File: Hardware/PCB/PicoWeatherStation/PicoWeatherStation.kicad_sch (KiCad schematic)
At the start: 40 parts, among them J1 TOUCH_PANEL, J2 LCD_BL, Q1 AO3400A, SW1 SW_PICO_RST, U1 Pico, U2 XPT2046, U3 nRF24L01+, U4 GY-BME280

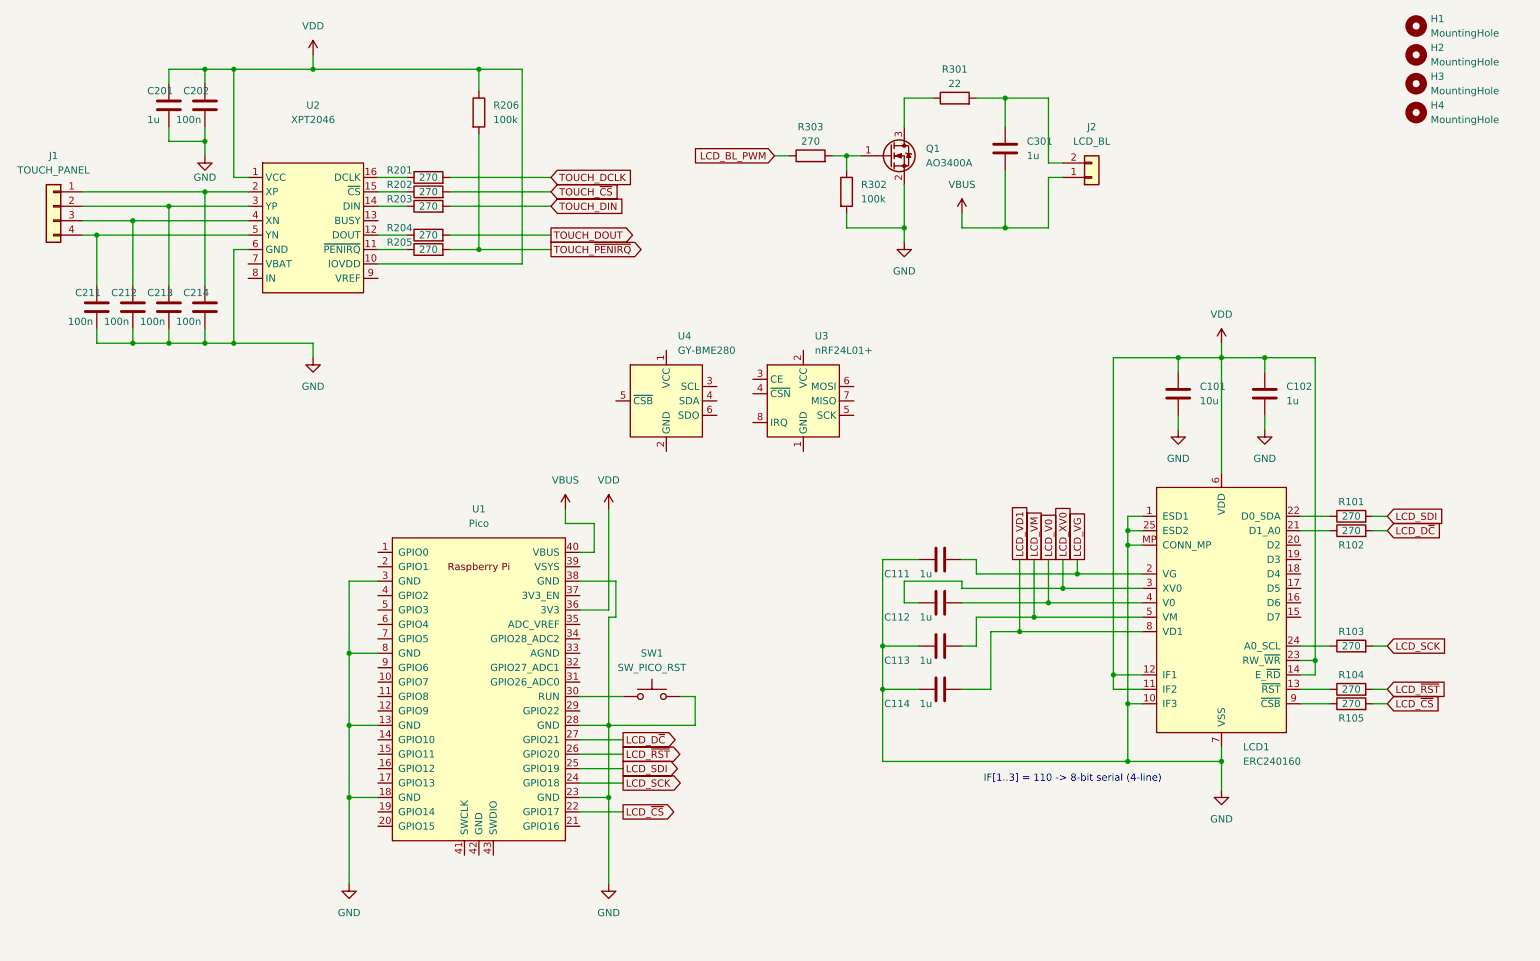
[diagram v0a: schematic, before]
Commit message: Fully wire up the PCB
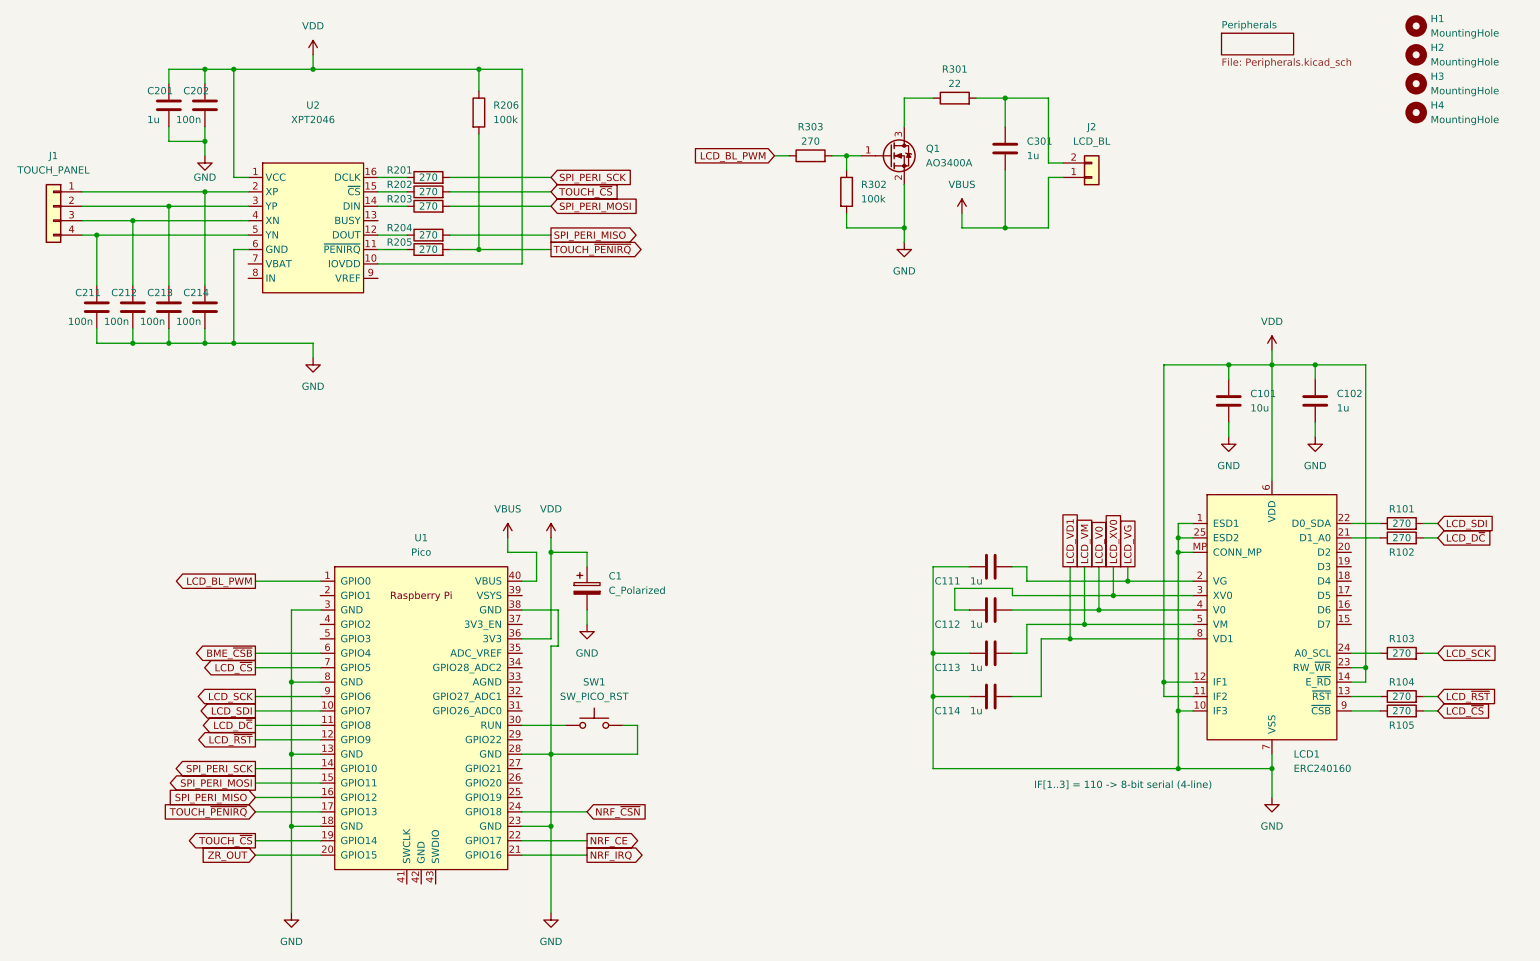
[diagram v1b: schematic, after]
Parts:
- removed U3: nRF24L01+, PicoWeatherStation:nRF24L01+, symbol PicoWeatherStation:nRF24L01+
- removed U4: GY-BME280, PicoWeatherStation:GY-BME280, symbol PicoWeatherStation:GY-BME280
- added C1: C_Polarized, Capacitor_SMD:CP_Elec_5x5.4, symbol Device:C_Polarized
- H1, H2, H3, H4: footprint MountingHole:MountingHole_3.2mm_M3_Pad_Via -> MountingHole:MountingHole_2.7mm_Pad_Via
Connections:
- net TOUCH_DCLK is gone; now on net SPI_PERI_SCK: R201.2
- net TOUCH_DIN is gone; now on net SPI_PERI_MOSI: R203.2
- net TOUCH_DOUT is gone; now on net SPI_PERI_MISO: R204.2
- net GND: now also C1.2
- net LCD_BL_PWM: now also U1.1 (GPIO0)
- net LCD_D~{C}: now also U1.11 (GPIO8); no longer U1.27 (GPIO21)
- net LCD_SCK: now also U1.9 (GPIO6); no longer U1.24 (GPIO18)
- net LCD_SDI: now also U1.10 (GPIO7); no longer U1.25 (GPIO19)
- net LCD_~{CS}: now also U1.7 (GPIO5); no longer U1.22 (GPIO17)
- net LCD_~{RST}: now also U1.12 (GPIO9); no longer U1.26 (GPIO20)
- net TOUCH_~{CS}: now also U1.19 (GPIO14)
- net TOUCH_~{PENIRQ}: now also U1.17 (GPIO13)
- net VDD: now also C1.1
- net SPI_PERI_SCK: now reaches U1.14 (GPIO10)
- net SPI_PERI_MOSI: now reaches U1.15 (GPIO11)
- net SPI_PERI_MISO: now reaches U1.16 (GPIO12)
- net ZR_OUT: now reaches U1.20 (GPIO15)
- net NRF_IRQ: now reaches U1.21 (GPIO16)
- net BME_~{CSB}: now reaches U1.6 (GPIO4)
- new net NRF_CE: U1.22 (GPIO17)
- new net NRF_~{CSN}: U1.24 (GPIO18)
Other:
- added sheet Peripherals (Peripherals.kicad_sch)
- moved on the sheet: C101, C102, C111, C112, C113, C114, LCD1, R101, R102, R103, R104, R105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

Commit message: Update the PCB
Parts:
- added R207: 270, Resistor_SMD:R_0805_2012Metric_Pad1.20x1.40mm_HandSolder, symbol Device:R
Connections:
- net ZR_OUT: now also U1.25 (GPIO19); no longer U1.20 (GPIO15)
- net at U2.13 (BUSY): now also R207.1
- new net TOUCH_BUSY: R207.2, U1.20 (GPIO15)
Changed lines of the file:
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@@
+    (stroke (width 0) (type default) (color 0 0 0 0))
+  )
+  (wire (pts (xy 106.68 153.67) (xy 118.11 153.67))
     (stroke (width 0) (type default) (color 0 0 0 0))
   )
@@
     (stroke (width 0) (type default) (color 0 0 0 0))
   )
+  (wire (pts (xy 81.28 52.07) (xy 86.36 52.07))
+    (stroke (width 0) (type default) (color 0 0 0 0))
+  )
   (wire (pts (xy 55.88 44.45) (xy 58.42 44.45))
     (stroke (width 0) (type default) (color 0 0 0 0))
@@
   )
   (wire (pts (xy 59.69 138.43) (xy 71.12 138.43))
+    (stroke (width 0) (type default) (color 0 0 0 0))
+  )
+  (wire (pts (xy 93.98 52.07) (xy 111.76 52.07))
     (stroke (width 0) (type default) (color 0 0 0 0))
   )
@@
     (effects (font (size 1.27 1.27)) (justify left bottom))
   )
-  (global_label "ZR_OUT" (shape input) (at 59.69 163.83 180) (fields_autoplaced)
+  (global_label "TOUCH_BUSY" (shape input) (at 59.69 163.83 180) (fields_autoplaced)
     (effects (font (size 1.27 1.27)) (justify right))
-    (property "Intersheet References" "${INTERSHEET_REFS}" (id 0) (at 50.2012 163.7506 0)
+    (property "Intersheet References" "${INTERSHEET_REFS}" (id 0) (at 45.1817 163.7506 0)
       (effects (font (size 1.27 1.27)) (justify right) hide)
     )
@@
     )
   )
+  (global_label "ZR_OUT" (shape input) (at 118.11 153.67 0) (fields_autoplaced)
+    (effects (font (size 1.27 1.27)) (justify left))
+    (property "Intersheet References" "${INTERSHEET_REFS}" (id 0) (at 127.5988 153.5906 0)
+      (effects (font (size 1.27 1.27)) (justify left) hide)
+    )
+  )
   (global_label "LCD_~{CS}" (shape input) (at 267.97 138.43 0) (fields_autoplaced)
     (effects (font (size 1.27 1.27)) (justify left))
@@
     (property "Intersheet References" "${INTERSHEET_REFS}" (id 0) (at 49.294 143.5894 0)
       (effects (font (size 1.27 1.27)) (justify right) hide)
+    )
+  )
+  (global_label "TOUCH_BUSY" (shape output) (at 111.76 52.07 0) (fields_autoplaced)
+    (effects (font (size 1.27 1.27)) (justify left))
+    (property "Intersheet References" "${INTERSHEET_REFS}" (id 0) (at 126.2683 51.9906 0)
+      (effects (font (size 1.27 1.27)) (justify left) hide)
     )
   )
@@
     )
     (property "Datasheet" "~" (id 3) (at 261.62 128.27 0)
+      (effects (font (size 1.27 1.27)) hide)
+    )
+    (pin "1")
+    (pin "2")
+  )
+  (symbol (lib_id "Device:R") (at 90.17 52.07 90) (unit 1)
+    (in_bom yes) (on_board yes)
+    (property "Reference" "R207" (id 0) (at 85.09 50.8 90))
+    (property "Value" "270" (id 1) (at 90.17 52.07 90))
+    (property "Footprint" "Resistor_SMD:R_0805_2012Metric_Pad1.20x1.40mm_HandSolder" (id 2) (at 90.17 53.848 90)
+      (effects (font (size 1.27 1.27)) hide)
+    )
+    (property "Datasheet" "~" (id 3) (at 90.17 52.07 0)
       (effects (font (size 1.27 1.27)) hide)
     )
@@
       (reference "R206") (unit 1) (value "100k") (footprint "Resistor_SMD:R_0805_2012Metric_Pad1.20x1.40mm_HandSolder")
     )
+    (path "/72400bf9-1560-4fc0-8dfb-0f046ef29e65"
+      (reference "R207") (unit 1) (value "270") (footprint "Resistor_SMD:R_0805_2012Metric_Pad1.20x1.40mm_HandSolder")
+    )
     (path "/8d763b0e-f6bf-4795-b6af-c73111e487f6"
       (reference "R301") (unit 1) (value "22") (footprint "Resistor_SMD:R_0805_2012Metric_Pad1.20x1.40mm_HandSolder")
@@
       (reference "SW1") (unit 1) (value "SW_PICO_RST") (footprint "Button_Switch_SMD:SW_Push_1P1T_NO_6x6mm_H9.5mm")
     )
+    (path "/8ed95ab6-c4d7-41f9-a767-b1e59c08f8aa/0dd8649c-8f2a-4391-b233-72bf55db379f"
+      (reference "SW2") (unit 1) (value "SW_PICO_RST") (footprint "Button_Switch_SMD:SW_Push_1P1T_NO_6x6mm_H9.5mm")
+    )
+    (path "/8ed95ab6-c4d7-41f9-a767-b1e59c08f8aa/ee07d6f4-6422-4982-b2c3-95f2866c5416"
+      (reference "SW3") (unit 1) (value "SW_PICO_RST") (footprint "Button_Switch_SMD:SW_Push_1P1T_NO_6x6mm_H9.5mm")
+    )
+    (path "/8ed95ab6-c4d7-41f9-a767-b1e59c08f8aa/31382075-085e-4e4a-ad7d-7fed5235aaa9"
+      (reference "SW4") (unit 1) (value "SW_PICO_RST") (footprint "Button_Switch_SMD:SW_Push_1P1T_NO_6x6mm_H9.5mm")
+    )
+    (path "/8ed95ab6-c4d7-41f9-a767-b1e59c08f8aa/e65e769d-e377-426b-848d-7c3769842a4d"
+      (reference "SW5") (unit 1) (value "SW_PICO_RST") (footprint "Button_Switch_SMD:SW_Push_1P1T_NO_6x6mm_H9.5mm")
+    )
+    (path "/8ed95ab6-c4d7-41f9-a767-b1e59c08f8aa/b6a0dc04-656d-4f3b-9f9e-ff27f7ab450f"
+      (reference "SW6") (unit 1) (value "SW_PICO_RST") (footprint "Button_Switch_SMD:SW_Push_1P1T_NO_6x6mm_H9.5mm")
+    )
+    (path "/8ed95ab6-c4d7-41f9-a767-b1e59c08f8aa/65b62161-ff71-4709-8b3d-3d54a8a02f6e"
+      (reference "SW7") (unit 1) (value "SW_PICO_RST") (footprint "Button_Switch_SMD:SW_Push_1P1T_NO_6x6mm_H9.5mm")
+    )
     (path "/8427f957-6735-4f61-a9c3-6b6f45bea61c"
       (reference "U1") (unit 1) (value "Pico") (footprint "RPi_Pico:RPi_Pico_SMD")
@@
       (reference "U5") (unit 1) (value "ZR-3A") (footprint "PicoWeatherStation:ZR-3A")
     )
-  )
+    (path "/8ed95ab6-c4d7-41f9-a767-b1e59c08f8aa/f7662088-e105-409d-894e-94e64f994389"
+      (reference "U6") (unit 1) (value "47L16") (footprint "Package_SO:SOIC-8_3.9x4.9mm_P1.27mm")
+    )
+    (path "/8ed95ab6-c4d7-41f9-a767-b1e59c08f8aa/a7682b72-4ff5-4db9-8a50-7573ecfde973"
+      (reference "U7") (unit 1) (value "MCP7940N-xSN") (footprint "Package_SO:SOIC-8_3.9x4.9mm_P1.27mm")
+    )
+  )

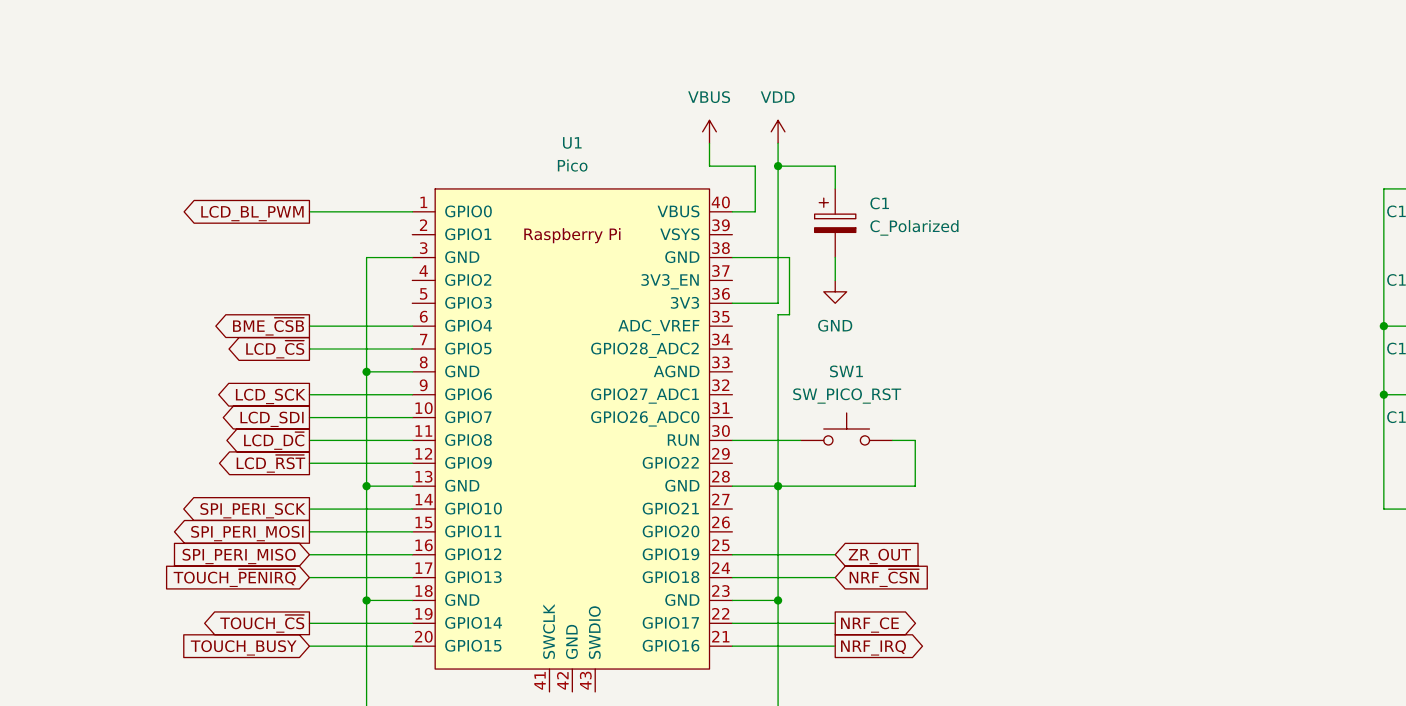
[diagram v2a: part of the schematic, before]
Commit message: PCB: add RTC and EERAM
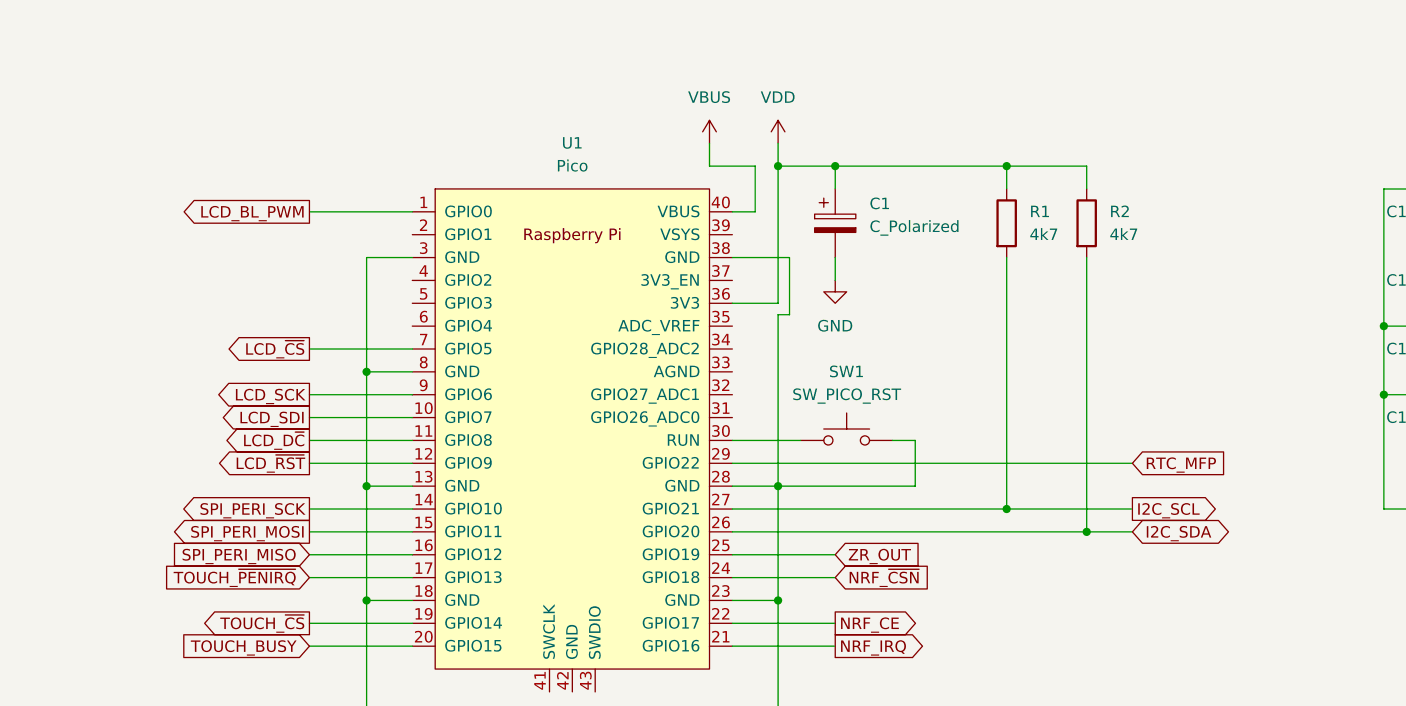
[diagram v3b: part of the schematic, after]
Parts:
- added R1, R2: 4k7, Resistor_SMD:R_0805_2012Metric_Pad1.20x1.40mm_HandSolder, symbol Device:R
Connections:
- net VDD: now also R1.1, R2.1
- net I2C_SDA: now reaches U1.26 (GPIO20)
- net I2C_SDA: now also R2.2
- net I2C_SCL: now reaches U1.27 (GPIO21)
- net I2C_SCL: now also R1.2
- net RTC_MFP: now reaches U1.29 (GPIO22)
- net BME_~{CSB}: no longer names the net of U1.6 (GPIO4)
